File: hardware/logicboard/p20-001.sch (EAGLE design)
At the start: 28 parts, among them IC11 74ALS04N, J0 DC9V, J11 AUDIO_JACK_3.5MM_PTH, J12 AUDIO_JACK_3.5MM_PTH, J13 AUDIO_JACK_3.5MM_PTH, J14 AUDIO_JACK_3.5MM_PTH, J7 DIN5, J8 DIN5, J9 DIN5, X0 MKDSN1,5/2-5,08

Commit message: Renumbered signals and parts.
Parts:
- renumbered L0 to L00, L1/2 to L0/1
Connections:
- net LED2 renamed LED0
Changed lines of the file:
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@@
 <part name="R10" library="rcl" library_urn="urn:adsk.eagle:library:334" deviceset="R-EU_" device="0204/5" package3d_urn="urn:adsk.eagle:package:23488/1"/>
 <part name="R2" library="rcl" library_urn="urn:adsk.eagle:library:334" deviceset="R-EU_" device="0204/5" package3d_urn="urn:adsk.eagle:package:23488/1"/>
-<part name="L0" library="led" library_urn="urn:adsk.eagle:library:259" deviceset="LED" device="3MM" package3d_urn="urn:adsk.eagle:package:15797/1" value="PWR"/>
+<part name="L00" library="led" library_urn="urn:adsk.eagle:library:259" deviceset="LED" device="3MM" package3d_urn="urn:adsk.eagle:package:15797/1" value="PWR"/>
 <part name="L2" library="led" library_urn="urn:adsk.eagle:library:259" deviceset="LED" device="3MM" package3d_urn="urn:adsk.eagle:package:15797/1" value="IN"/>
 <part name="L3" library="led" library_urn="urn:adsk.eagle:library:259" deviceset="LED" device="3MM" package3d_urn="urn:adsk.eagle:package:15797/1" value="OUT"/>
@@
 <part name="S1" library="switch-omron" library_urn="urn:adsk.eagle:library:377" deviceset="10-XX" device="" package3d_urn="urn:adsk.eagle:package:27496/1"/>
 <part name="JP6" library="pinhead" library_urn="urn:adsk.eagle:library:325" deviceset="PINHD-1X3" device="" package3d_urn="urn:adsk.eagle:package:22458/2"/>
-<part name="L1/2" library="led" library_urn="urn:adsk.eagle:library:259" deviceset="DUOLED-RG-C" device="" package3d_urn="urn:adsk.eagle:package:15851/1"/>
+<part name="L0/1" library="led" library_urn="urn:adsk.eagle:library:259" deviceset="DUOLED-RG-C" device="" package3d_urn="urn:adsk.eagle:package:15851/1"/>
 <part name="RN1" library="resistor-net" library_urn="urn:adsk.eagle:library:343" deviceset="RN04" device="" package3d_urn="urn:adsk.eagle:package:24976/1"/>
 <part name="SUPPLY2" library="supply2" deviceset="GND" device=""/>
@@
 <attribute name="VALUE" x="255.27" y="154.178" size="1.778" layer="96"/>
 </instance>
-<instance part="L0" gate="G$1" x="35.56" y="167.64" smashed="yes">
+<instance part="L00" gate="G$1" x="35.56" y="167.64" smashed="yes">
 <attribute name="NAME" x="39.116" y="163.068" size="1.778" layer="95" rot="R90"/>
 <attribute name="VALUE" x="41.275" y="163.068" size="1.778" layer="96" rot="R90"/>
@@
 <attribute name="VALUE" x="39.37" y="45.72" size="1.778" layer="96" rot="MR0"/>
 </instance>
-<instance part="L1/2" gate="G$1" x="58.42" y="170.18" smashed="yes">
+<instance part="L0/1" gate="G$1" x="58.42" y="170.18" smashed="yes">
 <attribute name="NAME" x="64.77" y="165.1" size="1.778" layer="95" rot="R90"/>
 <attribute name="VALUE" x="67.31" y="165.1" size="1.778" layer="96" rot="R90"/>
@@
 </segment>
 <segment>
-<pinref part="L0" gate="G$1" pin="C"/>
+<pinref part="L00" gate="G$1" pin="C"/>
 <wire x1="35.56" y1="162.56" x2="35.56" y2="160.02" width="0.1524" layer="91"/>
 <label x="35.56" y="160.02" size="0.8128" layer="95" rot="R270" xref="yes"/>
@@
 </segment>
 <segment>
-<pinref part="L1/2" gate="G$1" pin="C"/>
+<pinref part="L0/1" gate="G$1" pin="C"/>
 <wire x1="55.88" y1="170.18" x2="53.34" y2="170.18" width="0.1524" layer="91"/>
 <label x="53.34" y="170.18" size="0.8128" layer="95" rot="R180" xref="yes"/>
@@
 <segment>
 <pinref part="R10" gate="G$1" pin="1"/>
-<pinref part="L0" gate="G$1" pin="A"/>
+<pinref part="L00" gate="G$1" pin="A"/>
 <wire x1="35.56" y1="172.72" x2="35.56" y2="170.18" width="0.1524" layer="91"/>
 </segment>
@@
 </segment>
 </net>
-<net name="LED2" class="0">
+<net name="LED0" class="0">
 <segment>
 <pinref part="JP6" gate="A" pin="3"/>
@@
 <net name="N$3" class="0">
 <segment>
-<pinref part="L1/2" gate="G$1" pin="AR"/>
+<pinref part="L0/1" gate="G$1" pin="AR"/>
 <pinref part="R11" gate="G$1" pin="1"/>
 <wire x1="58.42" y1="177.8" x2="58.42" y2="180.34" width="0.1524" layer="91"/>
@@
 <net name="N$5" class="0">
 <segment>
-<pinref part="L1/2" gate="G$1" pin="AG"/>
+<pinref part="L0/1" gate="G$1" pin="AG"/>
 <pinref part="R12" gate="G$1" pin="2"/>
 <wire x1="58.42" y1="162.56" x2="58.42" y2="160.02" width="0.1524" layer="91"/>

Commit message: Renumbered parts.
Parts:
- removed R12: (no value), rcl:R-EU_0204/5
- added R00: (no value), rcl:R-EU_0204/5
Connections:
- net LED0: now also R11.1; no longer R12.1
- net LED1: now also R10.2; no longer R11.2
- net LEDPWR: now also R00.1; no longer R10.1
- net N$3: now also R10.1; no longer R11.1
- net N$5: now also R11.2; no longer R12.2
- net VCC/2: now also R00.2; no longer R10.2
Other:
- moved on the sheet: R10, R11
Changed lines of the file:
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@@
 <part name="J14" library="SparkFun-Connectors" library_urn="urn:adsk.eagle:library:513" deviceset="AUDIO_JACK_3.5MM" device="_PTH" package3d_urn="urn:adsk.eagle:package:37997/1"/>
 <part name="IC11" library="74xx-us" library_urn="urn:adsk.eagle:library:88" deviceset="74*04" device="N" package3d_urn="urn:adsk.eagle:package:16407/2" technology="ALS" value="74ALS04N"/>
-<part name="R10" library="rcl" library_urn="urn:adsk.eagle:library:334" deviceset="R-EU_" device="0204/5" package3d_urn="urn:adsk.eagle:package:23488/1"/>
+<part name="R00" library="rcl" library_urn="urn:adsk.eagle:library:334" deviceset="R-EU_" device="0204/5" package3d_urn="urn:adsk.eagle:package:23488/1"/>
 <part name="R2" library="rcl" library_urn="urn:adsk.eagle:library:334" deviceset="R-EU_" device="0204/5" package3d_urn="urn:adsk.eagle:package:23488/1"/>
 <part name="L00" library="led" library_urn="urn:adsk.eagle:library:259" deviceset="LED" device="3MM" package3d_urn="urn:adsk.eagle:package:15797/1" value="PWR"/>
@@
 <part name="SUPPLY2" library="supply2" deviceset="GND" device=""/>
 <part name="RN2" library="resistor-net" library_urn="urn:adsk.eagle:library:343" deviceset="RN04" device="" package3d_urn="urn:adsk.eagle:package:24976/1"/>
+<part name="R10" library="rcl" library_urn="urn:adsk.eagle:library:334" deviceset="R-EU_" device="0204/5" package3d_urn="urn:adsk.eagle:package:23488/1"/>
 <part name="R11" library="rcl" library_urn="urn:adsk.eagle:library:334" deviceset="R-EU_" device="0204/5" package3d_urn="urn:adsk.eagle:package:23488/1"/>
-<part name="R12" library="rcl" library_urn="urn:adsk.eagle:library:334" deviceset="R-EU_" device="0204/5" package3d_urn="urn:adsk.eagle:package:23488/1"/>
 </parts>
 <sheets>
@@
 <attribute name="VALUE" x="236.22" y="119.38" size="1.778" layer="96"/>
 </instance>
-<instance part="R10" gate="G$1" x="35.56" y="177.8" smashed="yes" rot="R90">
+<instance part="R00" gate="G$1" x="35.56" y="177.8" smashed="yes" rot="R90">
 <attribute name="NAME" x="34.0614" y="173.99" size="1.778" layer="95" rot="R90"/>
 <attribute name="VALUE" x="38.862" y="173.99" size="1.778" layer="96" rot="R90"/>
@@
 <attribute name="VALUE" x="167.64" y="122.682" size="1.778" layer="96"/>
 </instance>
-<instance part="R11" gate="G$1" x="58.42" y="185.42" smashed="yes" rot="R90">
+<instance part="R10" gate="G$1" x="58.42" y="185.42" smashed="yes" rot="R90">
 <attribute name="NAME" x="56.9214" y="181.61" size="1.778" layer="95" rot="R90"/>
 <attribute name="VALUE" x="61.722" y="181.61" size="1.778" layer="96" rot="R90"/>
 </instance>
-<instance part="R12" gate="G$1" x="58.42" y="154.94" smashed="yes" rot="R90">
+<instance part="R11" gate="G$1" x="58.42" y="154.94" smashed="yes" rot="R90">
 <attribute name="NAME" x="56.9214" y="151.13" size="1.778" layer="95" rot="R90"/>
 <attribute name="VALUE" x="61.722" y="151.13" size="1.778" layer="96" rot="R90"/>
@@
 </segment>
 <segment>
-<pinref part="R10" gate="G$1" pin="2"/>
+<pinref part="R00" gate="G$1" pin="2"/>
 <wire x1="35.56" y1="185.42" x2="35.56" y2="182.88" width="0.1524" layer="91"/>
 <label x="35.56" y="185.42" size="0.8128" layer="95" rot="R90" xref="yes"/>
@@
 <net name="LEDPWR" class="0">
 <segment>
-<pinref part="R10" gate="G$1" pin="1"/>
+<pinref part="R00" gate="G$1" pin="1"/>
 <pinref part="L00" gate="G$1" pin="A"/>
 <wire x1="35.56" y1="172.72" x2="35.56" y2="170.18" width="0.1524" layer="91"/>
@@
 </segment>
 <segment>
-<pinref part="R11" gate="G$1" pin="2"/>
+<pinref part="R10" gate="G$1" pin="2"/>
 <wire x1="58.42" y1="190.5" x2="58.42" y2="193.04" width="0.1524" layer="91"/>
 <label x="58.42" y="193.04" size="0.8128" layer="95" xref="yes"/>
@@
 </segment>
 <segment>
-<pinref part="R12" gate="G$1" pin="1"/>
+<pinref part="R11" gate="G$1" pin="1"/>
 <wire x1="58.42" y1="149.86" x2="58.42" y2="147.32" width="0.1524" layer="91"/>
 <label x="58.42" y="147.32" size="0.8128" layer="95" xref="yes"/>
@@
 <segment>
 <pinref part="L0/1" gate="G$1" pin="AR"/>
-<pinref part="R11" gate="G$1" pin="1"/>
+<pinref part="R10" gate="G$1" pin="1"/>
 <wire x1="58.42" y1="177.8" x2="58.42" y2="180.34" width="0.1524" layer="91"/>
 </segment>
@@
 <segment>
 <pinref part="L0/1" gate="G$1" pin="AG"/>
-<pinref part="R12" gate="G$1" pin="2"/>
+<pinref part="R11" gate="G$1" pin="2"/>
 <wire x1="58.42" y1="162.56" x2="58.42" y2="160.02" width="0.1524" layer="91"/>
 </segment>

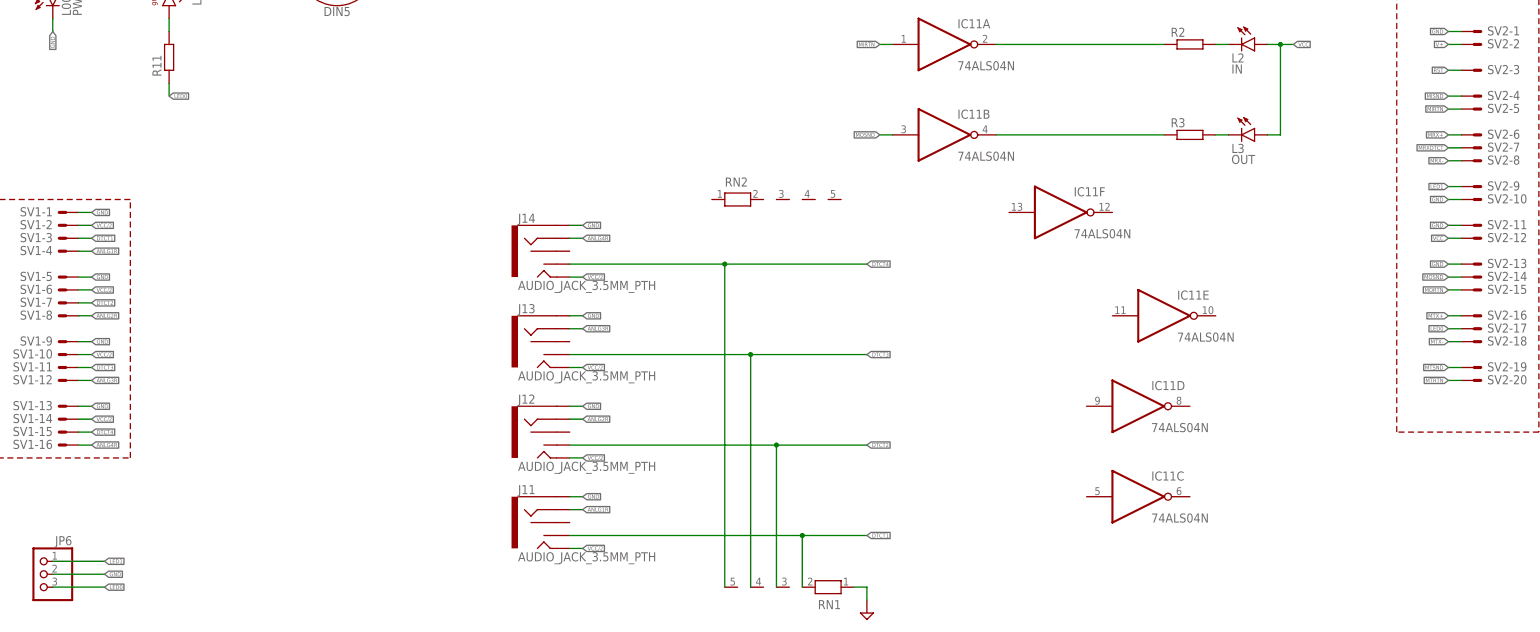
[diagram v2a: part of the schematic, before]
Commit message: Adopted to GeekPort II and BackPort II.
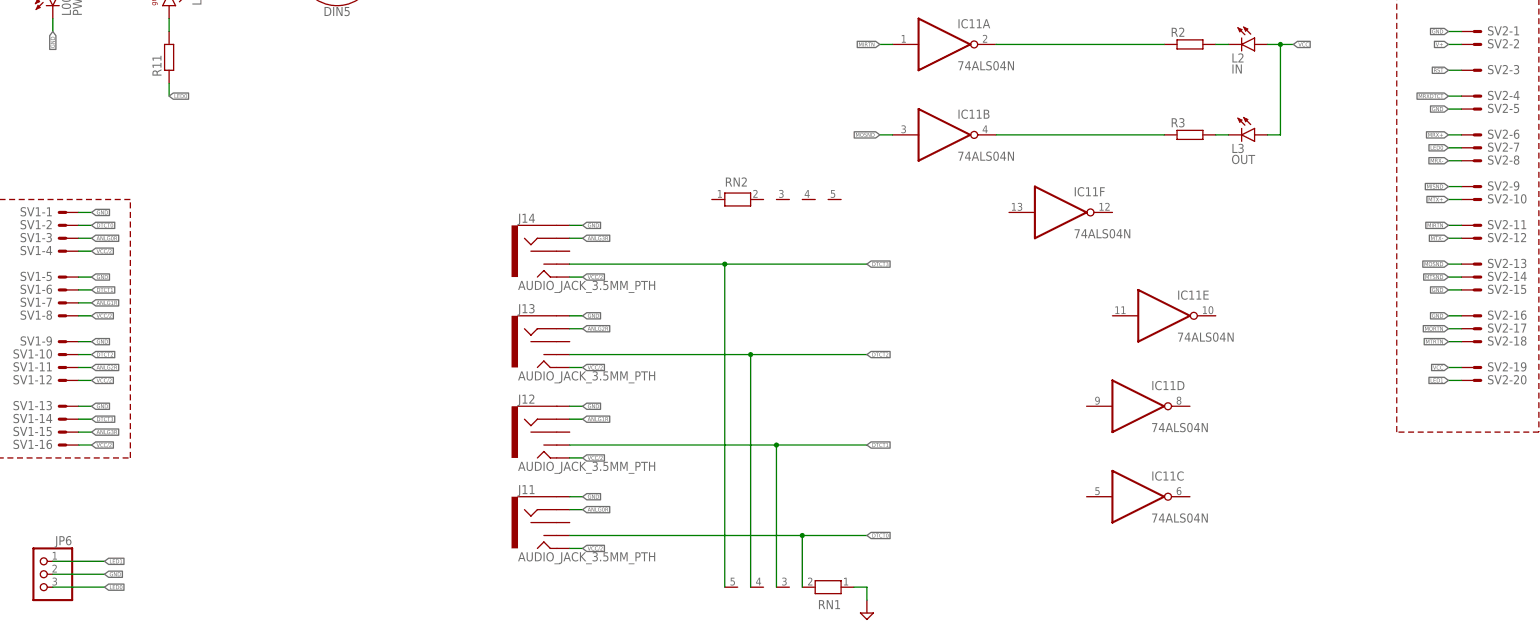
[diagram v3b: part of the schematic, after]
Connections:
- removed net ANLG4R: J14.RING, SV1-16.S
- removed net DTCT4: J14.TSH, RN1.5, SV1-15.S
- new net ANLG0R: J11.RING, SV1-3.S
- new net DTCT0: J11.TSH, RN1.2, SV1-2.S
- net ANLG1R: now also J12.RING, SV1-7.S; no longer J11.RING, SV1-4.S
- net ANLG2R: now also J13.RING, SV1-11.S; no longer J12.RING, SV1-8.S
- net ANLG3R: now also J14.RING, SV1-15.S; no longer J13.RING, SV1-12.S
- net DTCT1: now also J12.TSH, RN1.3, SV1-6.S; no longer J11.TSH, RN1.2, SV1-3.S
- net DTCT2: now also J13.TSH, RN1.4, SV1-10.S; no longer J12.TSH, RN1.3, SV1-7.S
- net DTCT3: now also J14.TSH, RN1.5, SV1-14.S; no longer J13.TSH, RN1.4, SV1-11.S
- net GND: now also SV2-15.S, SV2-16.S, SV2-5.S; no longer SV2-10.S, SV2-11.S, SV2-13.S
- net LED0: now also SV2-7.S; no longer SV2-17.S
- net LED1: now also SV2-20.S; no longer SV2-9.S
- net MIRTN: now also SV2-11.S; no longer SV2-5.S
- net MISND: now also SV2-9.S; no longer SV2-4.S
- net MORTN: now also SV2-17.S; no longer SV2-15.S
- net MOSND: now also SV2-13.S; no longer SV2-14.S
- net MRXDTCT: now also SV2-4.S; no longer SV2-7.S
- net MTRTN: now also SV2-18.S; no longer SV2-20.S
- net MTSND: now also SV2-14.S; no longer SV2-19.S
- net MTX+: now also SV2-10.S; no longer SV2-16.S
- net MTX-: now also SV2-12.S; no longer SV2-18.S
- net VCC: now also SV2-19.S; no longer SV2-12.S
- net VCC/2: now also SV1-12.S, SV1-16.S, SV1-4.S, SV1-8.S; no longer SV1-10.S, SV1-14.S, SV1-2.S, SV1-6.S

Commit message: Renamed signals.
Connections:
- net N$3 renamed LED1A
- net N$5 renamed LED0A
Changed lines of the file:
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@@
 </segment>
 </net>
-<net name="N$3" class="0">
+<net name="LED1A" class="0">
 <segment>
 <pinref part="L0/1" gate="G$1" pin="AR"/>
@@
 </segment>
 </net>
-<net name="N$5" class="0">
+<net name="LED0A" class="0">
 <segment>
 <pinref part="L0/1" gate="G$1" pin="AG"/>
